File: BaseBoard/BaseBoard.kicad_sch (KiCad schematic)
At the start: 44 parts, among them J1 USB_C_DEALON-USB-US31-106, J2 Serial Port, J3 base connector, Q1 PMN48XP, SW2 boot, SW3 Reset, U1 ESP32-WROOM-E, U3 MCP73831-2ACI-OT, U4 XC6210B332MR

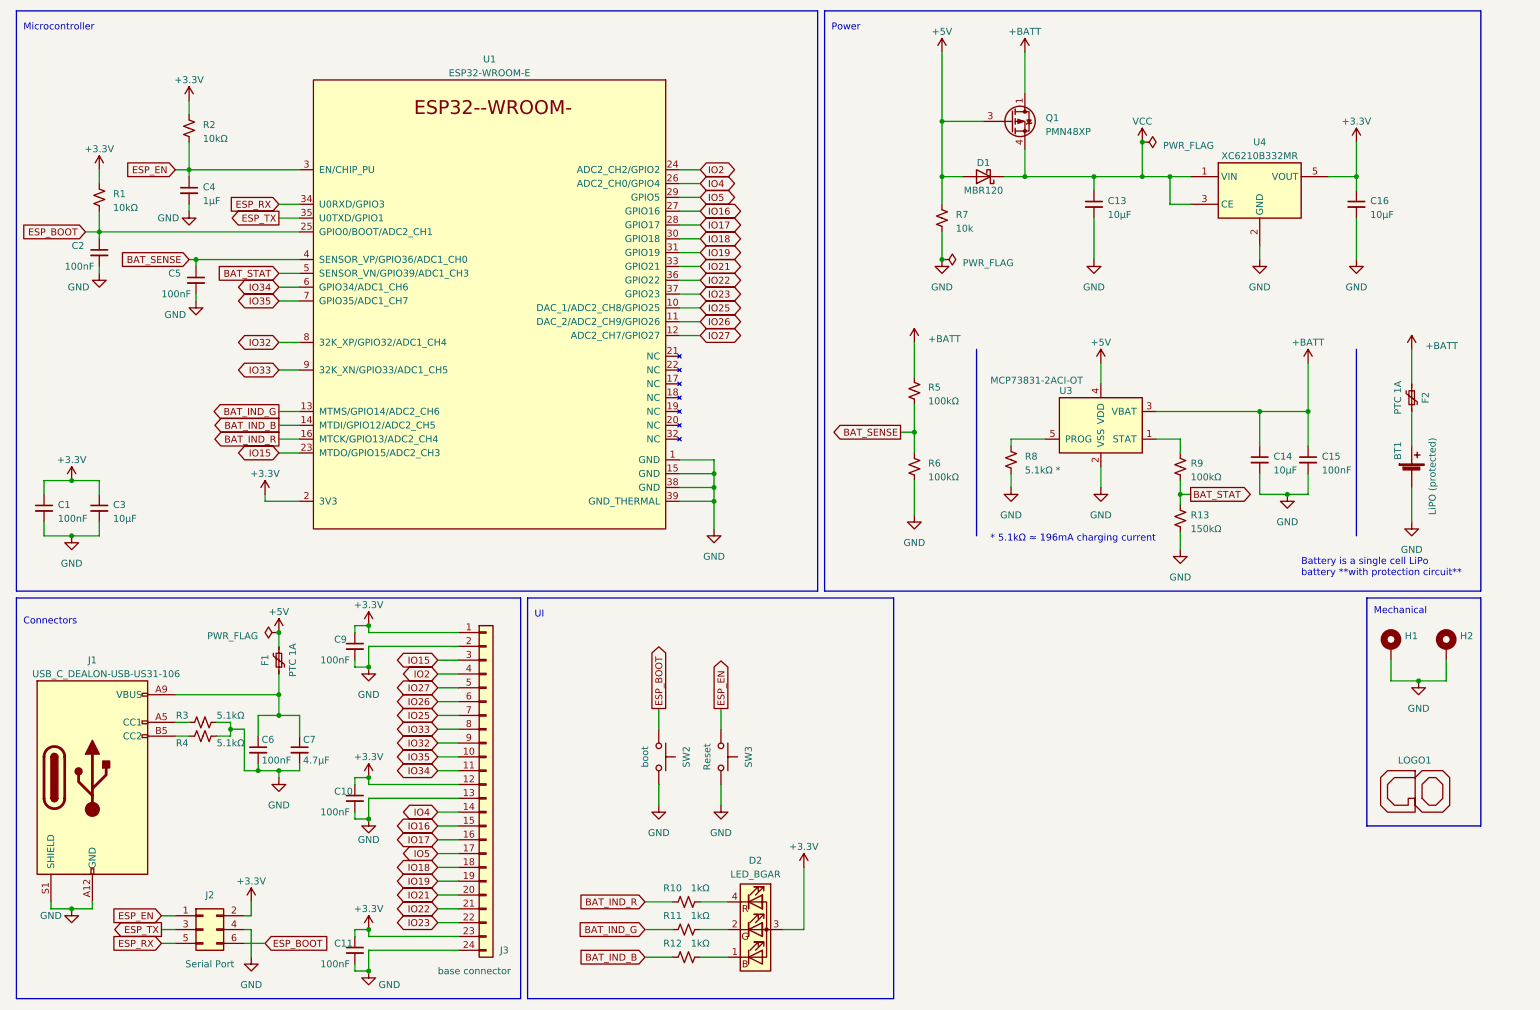
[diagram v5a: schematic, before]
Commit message: Adds soft power latching to schematics
The schematics is based on a design described in mosaic-industries
website[1]. The diode used is MBR120 for now since it's already in the
BOM, but it's quite an expensive diode where it's not needed, so we
might want to change it.

[1]: http://www.mosaic-industries.com/embedded-systems/microcontroller-projects/electronic-circuits/push-button-switch-turn-on/latching-toggle-power-switch#press-on-hold-off-latching-circuits
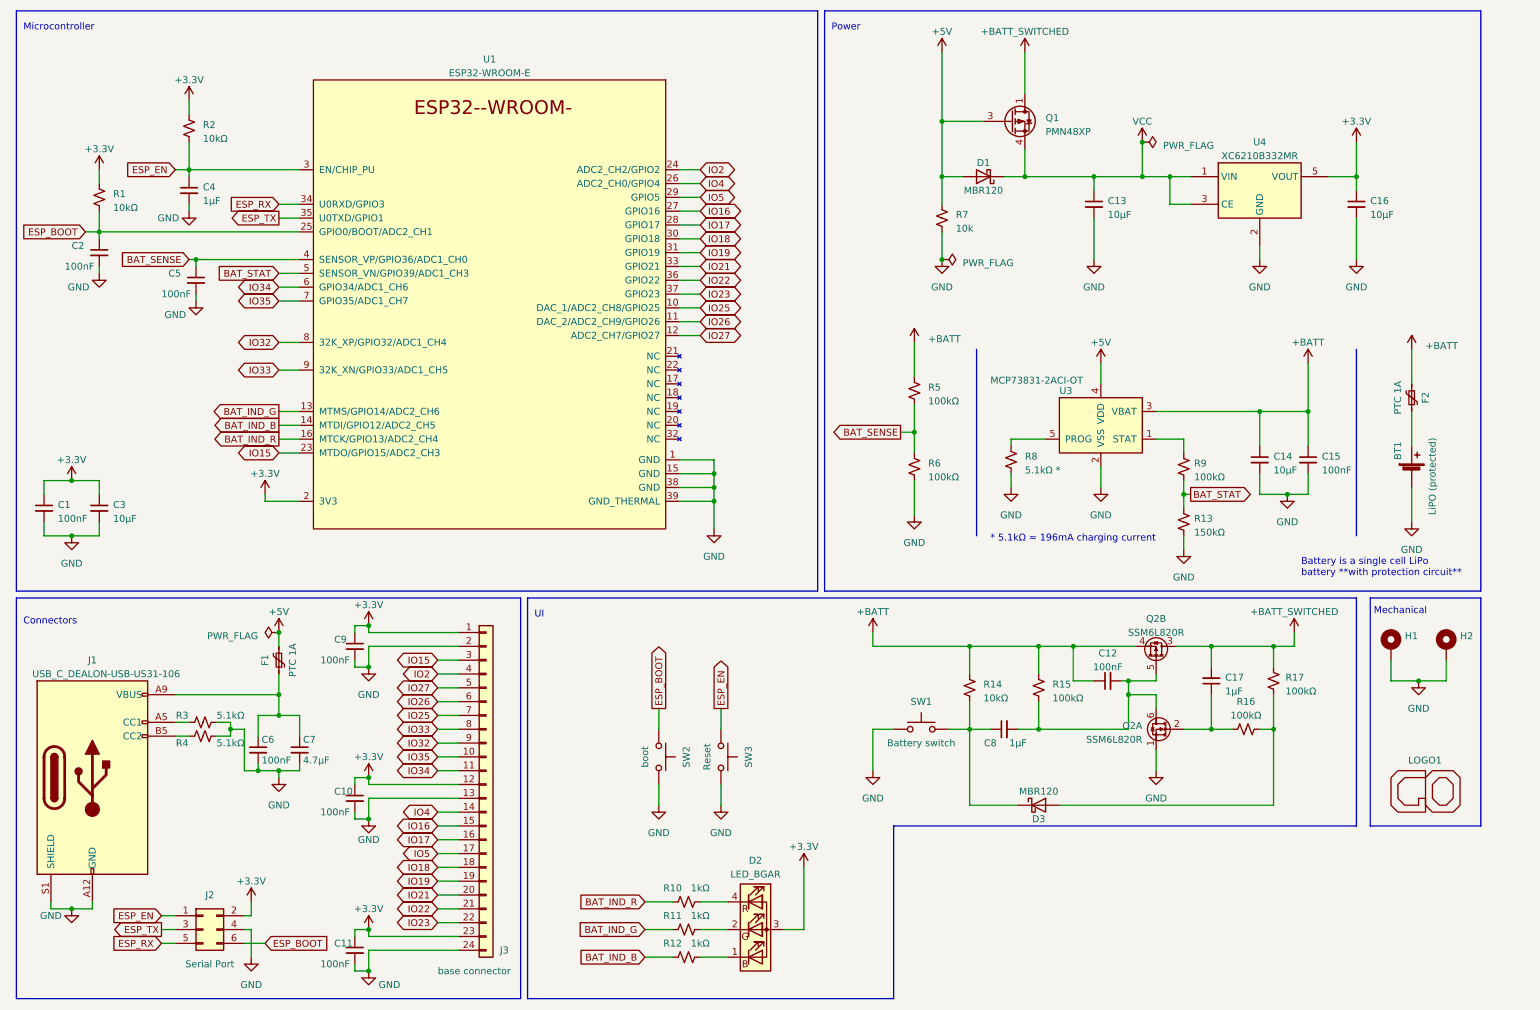
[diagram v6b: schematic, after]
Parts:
- added C12: 100nF, Capacitor_SMD:C_0805_2012Metric_Pad1.18x1.45mm_HandSolder, symbol Device:C_Small
- added C17, C8: 1µF, Capacitor_SMD:C_0805_2012Metric_Pad1.18x1.45mm_HandSolder, symbol Device:C_Small
- added D3: MBR120, Diode_SMD:D_SOD-123, symbol Device:D_Schottky
- added Q2: SSM6L820R, GameOver:TSOP6F, symbol GameOver:SSM6L820R
- added R14: 10kΩ, Resistor_SMD:R_0805_2012Metric_Pad1.20x1.40mm_HandSolder, symbol Device:R_Small_US
- added R15, R16, R17: 100kΩ, Resistor_SMD:R_0805_2012Metric_Pad1.20x1.40mm_HandSolder, symbol Device:R_Small_US
- added SW1: Battery switch, GameOver:SW_Tactile_SPST_SOFNG_TS-1814, symbol Switch:SW_Push
- LOGO1: value (none) -> GameOver_logo; footprint (none) -> GameOver:logo_fsilk
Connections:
- net +BATT: now also C12.1, C17.2, Q2.3 (D), Q2.4 (S), R14.1, R15.1, R17.2
- net GND: now also Q2.1 (S), SW1.1
- new net: C8.1, D3.1 (K), R14.2, SW1.2
- new net: C17.1, Q2.2 (G), R16.1
- new net: C12.2, C8.2, Q2.5 (G), Q2.6 (D), R15.2
- new net: D3.2 (A), R16.2, R17.1
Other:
- moved on the sheet: LOGO1, R13, R9
